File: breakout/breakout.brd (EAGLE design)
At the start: 485 x 130 mm, 229 parts, among them J15 1789472, J16 1789472, J27 69168-124HLF, J30 SJ1-3514-SMT-TR, J32 69168-116HLF, J33 12226-8250-00FR, J34 1888276, J35 69168-116HLF, J36 1888276, Q1 SI1012R, Q2 SI1012R, Q3 SI1012R, Q4 SI1012R, U1 SK6805-E-J, U10 TXB0101, U11 SK6805-E-J, U12 SK6805-E-J, U13 SK6805-E-J, U14 SK6805-E-J, U15 SK6805-E-J, U16 SK6805-E-J, U17 SK6805-E-J, U18 SK6805-E-J, U19 SK6805-E-J, U2 SK6805-E-J, U20 SK6805-E-J, U21 SK6805-E-J, U22 SK6805-E-J, U23 SK6805-E-J, U24 SK6805-E-J, U25 SK6805-E-J, U26 SK6805-E-J, U27 SK6805-E-J, U28 SK6805-E-J, U29 SK6805-E-J, U3 SK6805-E-J, U30 SK6805-E-J, U31 SK6805-E-J, U32 SK6805-E-J, U33 SK6805-E-J, U34 SK6805-E-J, U35 SK6805-E-J, U36 SK6805-E-J, U37 SK6805-E-J, U38 SK6805-E-J, U39 SK6805-E-J, U4 SK6805-E-J, U40 SK6805-E-J, U41 SK6805-E-J, U42 SK6805-E-J, U43 G6K-2F-RF, U44 G6K-2F-RF, U45 G6K-2F-RF, U46 G6K-2F-RF, U47 LTM4622A, U48 SI8610, U49 TINY-FPGA-BX, U5 SK6805-E-J, U50 TCA9555, U51 FIN1032MTCX, U52 SN65LVDS9638DGN, U53 SN65LVDS9638DGN, U6 SK6805-E-J, U7 SK6805-E-J, U8 SK6805-E-J, U9 SK6805-E-J

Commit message: Initial commit of breakout rev 1.4
- Fixes to analog routing to maintain consistancy of analog and digital
pin ordering in the screw terminals and IDC headers
- Switch the ordering of BNC analog connector to row major and aligned
in column direction.
- Add a secondary, internally controlled FET in series with the coil on
each headstage relay so that certain ports can be disabled when
instructed from host.
- Changed the optical table mounting holes to slots that can accomidate
both metric and imperial spacing.
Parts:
- added Q5, Q6, Q7, Q8: SI1012R, jonnew:SC75
- added R35, R37, R39, R41: 100k, jonnew:0402
- added R36, R38, R40, R42: 1k, jonnew:0402
- R11: value 12.5k -> 13.3k
- moved J14 120.8 mm to (240.0, 90.0)
- moved J21 120.8 mm to (40.0, 40.0)
- moved D10 118.8 mm to (260.0, 87.5), turned to 90 degrees
- moved D11 118.8 mm to (60.0, 42.5), turned to 270 degrees
- moved D12 90.0 mm to (100.0, 42.5)
- moved D9 90.0 mm to (220.0, 87.5)
- moved J13 90.0 mm to (200.0, 90.0)
- moved J22 90.0 mm to (80.0, 40.0)
- moved J12 86.0 mm to (160.0, 90.0)
- moved J23 86.0 mm to (120.0, 40.0)
- moved D13 83.2 mm to (140.0, 42.5), turned to 270 degrees
- moved D8 83.2 mm to (180.0, 87.5), turned to 90 degrees
- moved J10 58.3 mm to (80.0, 90.0)
- moved J25 58.3 mm to (200.0, 40.0)
- moved D15 54.1 mm to (220.0, 42.5), turned to 270 degrees
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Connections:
- removed net N$39: D4.C, Q4.2, U46.1
- removed net RELAY_SENSE_0: C28.2, Q1.1, R3.2, U50.6
- removed net RELAY_SENSE_1: C29.2, Q2.1, R4.1, U50.5
- removed net RELAY_SENSE_2: C30.2, Q3.1, R5.1, U50.4
- removed net RELAY_SENSE_3: C31.2, Q4.1, R6.1, U50.20
- new net N$12: D2.A, Q2.3, U44.7
- new net N$50: D3.A, Q3.3, U45.7
- new net N$59: D4.A, Q4.3, U46.7
- new net N$6: Q1.2, Q5.3
- new net N$60: Q4.2, Q8.3
- new net RELAY_AND_0: Q5.1, R36.2, U50.8
- new net RELAY_AND_1: Q6.1, R38.2, U50.6
- new net RELAY_AND_2: Q7.1, R40.2, U50.4
- new net RELAY_AND_3: Q8.1, R42.2, U50.20
- new net RELAY_MECH_0: C28.2, Q1.1, R3.2, R35.2, U50.9
- new net RELAY_MECH_1: C29.2, Q2.1, R37.2, R4.1, U50.7
- new net RELAY_MECH_2: C30.2, Q3.1, R39.2, R5.1, U50.5
- new net RELAY_MECH_3: C31.2, Q4.1, R41.2, R6.1, U50.19
- net +5V0: now also D1.C, D2.C, D3.C, D4.C, U43.1, U44.1, U45.1, U46.1; no longer Q1.3, Q2.3, Q3.3, Q4.3
- net AIO_0: now also J27.2; no longer J27.24
- net AIO_1: now also J27.4; no longer J27.22
- net AIO_10: now also J27.22; no longer J27.4
- net AIO_11: now also J27.24; no longer J27.2
- net AIO_2: now also J27.6; no longer J27.20
- net AIO_3: now also J27.8; no longer J27.18
- net AIO_4: now also J27.10; no longer J27.16
- net AIO_5: now also J27.12; no longer J27.14
- net AIO_6: now also J27.14; no longer J27.12
- net AIO_7: now also J27.16; no longer J27.10
- net AIO_8: now also J27.18; no longer J27.8
- net AIO_9: now also J27.20; no longer J27.6
- net BUTTON1: now also S8.SW1, U50.17; no longer S5.SW1, U50.9
- net BUTTON2: now also S10.SW1, U50.18; no longer S8.SW1, U50.17
- net BUTTON3: now also S5.SW1, U50.11; no longer S7.SW1, U50.14
- net BUTTON4: now also S7.SW1, U50.14; no longer S10.SW1, U50.18
- net BUTTON5: now also U50.10; no longer U50.8
- net GND: now also Q5.2, Q6.2, Q7.2, Q8.2, R35.1, R36.1, R37.1, R38.1, R39.1, R40.1, R41.1, R42.1; no longer D1.A, D2.A, D3.A, D4.A, U43.7, U44.7, U45.7, U46.7
- net N$32: now also Q7.3; no longer D3.C, U45.1
- net N$40: now also Q6.3; no longer D2.C, U44.1
- net N$5: now also D1.A, Q1.3, U43.7; no longer D1.C, Q1.2, U43.1
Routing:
- net RELAY_SENSE_0: track 167.7 -> 0.00 mm, vias 2 -> 0
- net RELAY_MECH_0: track 0.00 -> 164.2 mm, vias 0 -> 4
- net RELAY_AND_0: track 0.00 -> 154.3 mm, vias 0 -> 3
- net AIO_5: track 436.0 -> 282.2 mm, vias 3 -> 2
- net RELAY_MECH_1: track 0.00 -> 149.8 mm, vias 0 -> 4
- net RELAY_MECH_3: track 0.00 -> 145.9 mm, vias 0 -> 4
- net RELAY_AND_1: track 0.00 -> 145.0 mm, vias 0 -> 3
- net RELAY_SENSE_1: track 144.9 -> 0.00 mm, vias 2 -> 0
- net RELAY_AND_3: track 0.00 -> 141.6 mm, vias 0 -> 3
- net RELAY_SENSE_3: track 135.9 -> 0.00 mm, vias 2 -> 0
- net RELAY_MECH_2: track 0.00 -> 130.0 mm, vias 0 -> 4
- net AIO_6: track 400.3 -> 529.8 mm
- net RELAY_AND_2: track 0.00 -> 123.8 mm, vias 0 -> 3
- net RELAY_SENSE_2: track 122.7 -> 0.00 mm, vias 2 -> 0
- net AIO_3: track 471.0 -> 372.4 mm
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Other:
- outline, holes or cut-outs redrawn
- board text added: "(18", 0")"
- board text added: "(200,0)"
- board text added: "(200,100)"
- board text added: "(450,0)"
- board text added: "(8",0")"
- board text added: "Rev. 1.4 CC BY-NC-SA 4.0 JPN, JV, MIT 2019"
- board text removed: "(0",0")"
- board text removed: "(17", 0")"
- board text removed: "(225,0)"
- board text removed: "(425,0)"
- board text removed: "Rev. 1.3 CERN OHL v1.2 JPN, JV, MIT 2019"

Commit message: Changes to breakout rev 1.4 after case fit test with rev 1.3
- Moved components to prevent them from being smashed by case
- More clearance around M3 holes
- Smaller font on analog BNC labels
- Moved the terminal blocks so that there spacing makes more sense for
related signals.
- Modeled screw terminal blocks correctly
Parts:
- removed TP8: (no value), jonnew:TP19R
- R11: value 13.3k -> 1k
- R12: value 649k -> 100k
- R13: value 8.25k -> 1k
- R14, R16: value 4.7k -> 100k
- R15: value 4.7k -> 1k
- R17: value 100 -> 1k
- R18: value 100 -> 100k
- R19: value 270, 0.5W -> 13.3k; device jonnew:0805 -> jonnew:0402
- R20: value 270, 0.5W -> 649k; device jonnew:0805 -> jonnew:0402
- R21: value 270, 0.5W -> 8.25k; device jonnew:0805 -> jonnew:0402
- R22, R23, R24: value 270, 0.5W -> 4.7k; device jonnew:0805 -> jonnew:0402
- R25, R26: value 270, 0.5W -> 100; device jonnew:0805 -> jonnew:0402
- R35, R37, R39, R41: value 100k -> 270, 0.5W; device jonnew:0402 -> jonnew:0805
- R36, R38, R40, R42: value 1k -> 270, 0.5W; device jonnew:0402 -> jonnew:0805
- TP7: device jonnew:TESTPOINT_2MM -> jonnew:TP19R
- moved TP7 228.0 mm to (456.1, 78.2)
- moved R35 178.2 mm to (469.3, 111.3), turned to 180 degrees
- moved R37 168.1 mm to (472.9, 111.3), turned to 180 degrees
- moved TP5 164.3 mm to (295.0, 4.90)
- moved R39 163.1 mm to (476.5, 111.3), turned to 180 degrees
- moved R41 161.9 mm to (480.1, 111.3), turned to 180 degrees
- moved R36 148.2 mm to (432.9, 114.4), turned to 180 degrees
- moved R12 138.3 mm to (317.4, 18.1), turned to 90 degrees
- moved R18 137.9 mm to (319.2, 93.3)
- moved R11 136.5 mm to (320.2, 18.1), turned to 90 degrees
- moved R17 135.3 mm to (322.0, 93.3), turned to 90 degrees
- moved R13 133.9 mm to (322.0, 43.3), turned to 90 degrees
- moved R38 129.6 mm to (432.9, 110.4), turned to 180 degrees
- moved R15 128.2 mm to (322.0, 68.2), turned to 90 degrees
- moved R16 127.2 mm to (319.2, 68.2), turned to 90 degrees
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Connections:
- net !TCA_INT: now also R22.2; no longer R14.2
- net +12V: now also TP7.TP; no longer TP8.TP
- net +3V3: now also R22.1, R23.1, R24.1; no longer R14.1, R15.1, R16.1
- net AGND: now also TP6.1; no longer TP7.1
- net BUTTON0: now also S5.SW1; no longer S6.SW1
- net BUTTON1: now also S7.SW1; no longer S8.SW1
- net BUTTON2: now also S9.SW1; no longer S10.SW1
- net BUTTON3: now also S6.SW1; no longer S5.SW1
- net BUTTON4: now also S8.SW1; no longer S7.SW1
- net BUTTON5: now also S10.SW1; no longer S9.SW1
- net DIN0: now also R42.2; no longer R34.2
- net DIN0_P: now also R42.1; no longer R34.1
- net DIN1: now also R34.2; no longer R26.2
- net DIN1_P: now also R34.1; no longer R26.1
- net DIN2: now also R40.2; no longer R32.2
- net DIN2_P: now also R40.1; no longer R32.1
- net DIN3: now also R32.2; no longer R24.2
- net DIN3_P: now also R32.1; no longer R24.1
- net DIN4: now also R38.2; no longer R30.2
- net DIN4_P: now also R38.1; no longer R30.1
- net DIN5: now also R30.2; no longer R22.2
- net DIN5_P: now also R30.1; no longer R22.1
- net DIN6: now also R36.2; no longer R28.2
- net DIN6_P: now also R36.1; no longer R28.1
- net DIN7: now also R28.2; no longer R20.2
- net DIN7_P: now also R28.1; no longer R20.1
- net DOUT0: now also D21.2, R27.2; no longer D21.10, R19.2
- net DOUT0_P: now also R27.1; no longer R19.1
- net DOUT1: now also D21.1, R29.2; no longer D21.9, R21.2
- net DOUT1_P: now also R29.1; no longer R21.1
- net DOUT2: now also D21.3, R31.2; no longer D21.2, R23.2
- net DOUT2_P: now also R31.1; no longer R23.1
- net DOUT3: now also D21.4, R33.2; no longer D21.7, R25.2
- net DOUT3_P: now also R33.1; no longer R25.1
- net DOUT4: now also D21.10, R35.2; no longer D21.3, R27.2
- net DOUT4_P: now also R35.1; no longer R27.1
- net DOUT5: now also D21.9, R37.2; no longer D21.6, R29.2
- net DOUT5_P: now also R37.1; no longer R29.1
- net DOUT6: now also D21.7, R39.2; no longer D21.4, R31.2
- net DOUT6_P: now also R39.1; no longer R31.1
- net DOUT7: now also D21.6, R41.2; no longer D21.1, R33.2
- net DOUT7_P: now also R41.1; no longer R33.1
- net GND: now also R11.1, R12.1, R13.1, R14.1, R15.1, R16.1, R17.1, R18.1, R19.2, R20.2, R21.2; no longer R11.2, R12.2, R13.2, R35.1, R36.1, R37.1, R38.1, R39.1, R40.1, R41.1, R42.1, TP6.1
- net I2C_SCL: now also R23.2; no longer R15.2
- net I2C_SDA: now also R24.2; no longer R16.2
- net LVDS_DOUT0_N: now also R25.1; no longer R17.1
- net LVDS_DOUT0_P: now also R25.2; no longer R17.2
- net LVDS_DOUT1_N: now also R26.1; no longer R18.1
- net LVDS_DOUT1_P: now also R26.2; no longer R18.2
- net N$145: now also R20.1; no longer R12.1
- net N$24: now also R21.1; no longer R13.1
- net N$25: now also R19.1; no longer R11.1
- net RELAY_AND_0: now also R11.2; no longer R36.2
- net RELAY_AND_1: now also R13.2; no longer R38.2
- net RELAY_AND_2: now also R15.2; no longer R40.2
- net RELAY_AND_3: now also R17.2; no longer R42.2
- net RELAY_MECH_0: now also R12.2; no longer R35.2
- net RELAY_MECH_1: now also R14.2; no longer R37.2
- net RELAY_MECH_2: now also R16.2; no longer R39.2
- net RELAY_MECH_3: now also R18.2; no longer R41.2
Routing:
- net DOUT7: track 63.8 -> 86.6 mm
- net DOUT6: track 63.4 -> 83.4 mm
- net DIN1: track 93.6 -> 83.7 mm
- net DIN0: track 82.8 -> 73.2 mm
- net DIN4: track 68.6 -> 61.2 mm
- net DOUT1: track 52.6 -> 45.8 mm
- net DIN6: track 64.3 -> 57.9 mm
- net DIN5: track 74.3 -> 68.1 mm
- net DIN2: track 73.7 -> 67.6 mm
- net DOUT3: track 62.7 -> 56.6 mm
- net DOUT4: track 65.0 -> 70.6 mm
- net DIN3: track 80.7 -> 75.1 mm
- net DOUT5: track 69.1 -> 74.1 mm
- net DOUT0: track 48.8 -> 44.4 mm
- net DOUT1_P: track 6.23 -> 9.69 mm
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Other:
- board text added: "GPIO"
- board text removed: "DIGITAL IO"

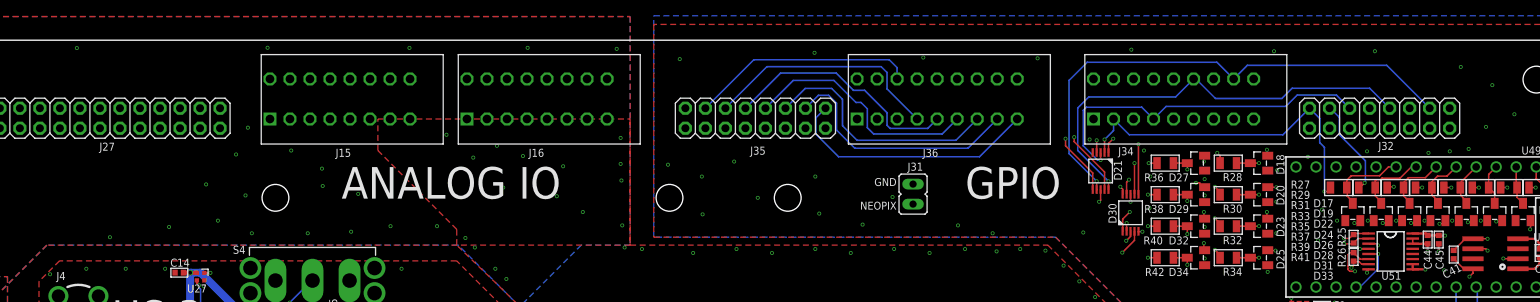
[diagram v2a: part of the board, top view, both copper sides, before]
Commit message: Minore updates to breakout rev 1.4
- Address issues found during the construction of the case
- DOUT IDC and terminal block switch positions to match the other two IO
banks
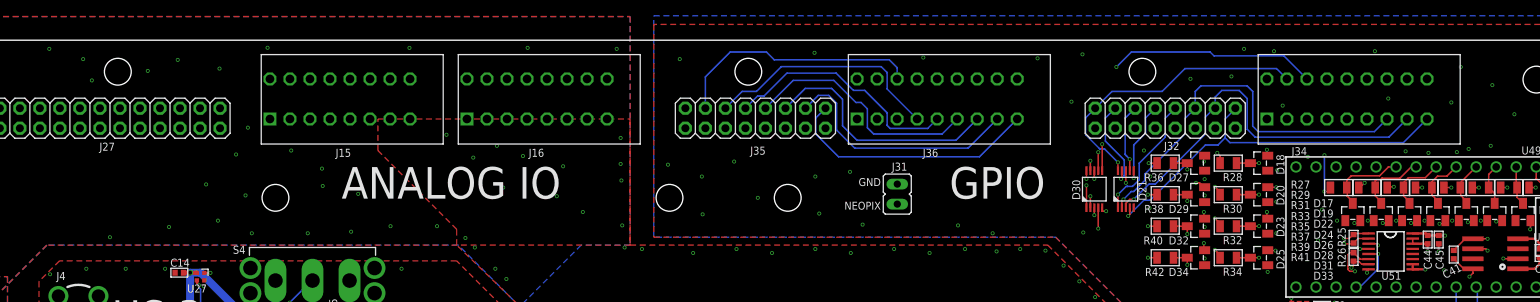
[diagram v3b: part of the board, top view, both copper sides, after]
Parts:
- moved J32 27.2 mm to (432.9, 120.0)
- moved J34 22.0 mm to (445.8, 120.0)
- moved D30 5.49 mm to (423.9, 111.1)
- moved D21 3.94 mm to (427.9, 111.1), turned to 90 degrees
- moved J31 2.00 mm to (398.9, 109.2)
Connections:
- net DOUT0: now also D21.10; no longer D21.2
- net DOUT1: now also D21.9; no longer D21.1
- net DOUT2: now also D21.7; no longer D21.3
- net DOUT3: now also D21.6; no longer D21.4
- net DOUT4: now also D21.1; no longer D21.10
- net DOUT5: now also D21.2; no longer D21.9
- net DOUT6: now also D21.3; no longer D21.7
- net DOUT7: now also D21.4; no longer D21.6
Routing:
- net DOUT7: track 86.6 -> 70.6 mm
- net DOUT6: track 83.4 -> 70.6 mm
- net DOUT4: track 70.6 -> 58.3 mm
- net DOUT1: track 45.8 -> 56.9 mm, vias 2 -> 3
- net DOUT2: track 58.1 -> 50.4 mm
- net DOUT5: track 74.1 -> 66.6 mm
- net DOUT0: track 44.4 -> 50.0 mm, vias 2 -> 3
- net DOUT3: track 56.6 -> 51.6 mm
- net DIN7: track 68.1 -> 64.5 mm
- net DIN1: track 83.7 -> 87.1 mm
- net DIN0: track 73.2 -> 75.9 mm
- net NEOPIXEL_DIN: track 53.8 -> 55.8 mm
- net DIN6: track 57.9 -> 56.2 mm
- net AIO_2: track 411.6 -> 413.0 mm
- net AIO_0: track 485.5 -> 484.2 mm
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
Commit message: More updates to breakout rev. 1.4 to fit case
- Swiched 2x 8 pin screw terminals for a single 16 pin screw terminal.
- Moved m3 clearance holes in front of IDC connectors up a bit
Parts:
- removed J36: 1888276, jonnew:SCREW9-2
- J15: value 1789472 -> (none); device jonnew:SCREW8-2 -> jonnew:MMCX-THRU
- J16: value 1789472 -> (none); device jonnew:SCREW8-2 -> jonnew:SMA_JACK_142-0701-201
- J17: value (none) -> 1789074; device jonnew:MMCX-THRU -> jonnew:SCREW16-2
- J18: device jonnew:SMA_JACK_142-0701-201 -> jonnew:MMCX-THRU
- J19, J28: device jonnew:MMCX-THRU -> jonnew:SMA_JACK_142-0701-201
- J20: device jonnew:SMA_JACK_142-0701-201 -> jonnew:0731010360
- J26: value (none) -> 69168-124HLF; device jonnew:0731010360 -> jonnew:2X12-BIG
- J27: value 69168-124HLF -> (none); device jonnew:2X12-BIG -> jonnew:MMCX-THRU
- J29: value (none) -> SJ1-3514-SMT-TR; device jonnew:SMA_JACK_142-0701-201 -> jonnew:35RASMT2BHNTRX
- J30: value SJ1-3514-SMT-TR -> (none); device jonnew:35RASMT2BHNTRX -> jonnew:JP2
- J31: value (none) -> 69168-116HLF; device jonnew:JP2 -> jonnew:2X08-BIG
- J32: value 69168-116HLF -> 12226-8250-00FR; device jonnew:2X08-BIG -> jonnew:12226-82X0-00XX
- J33: value 12226-8250-00FR -> 1888276; device jonnew:12226-82X0-00XX -> jonnew:SCREW9-2
- J34: value 1888276 -> 69168-116HLF; device jonnew:SCREW9-2 -> jonnew:2X08-BIG
- J35: value 69168-116HLF -> 1888276; device jonnew:2X08-BIG -> jonnew:SCREW9-2
- moved J20 340.6 mm to (40.0, 40.0)
- moved J27 211.8 mm to (480.0, 10.0)
- moved J17 190.4 mm to (318.0, 120.0)
- moved J15 189.3 mm to (480.0, 20.0)
- moved J29 139.3 mm to (479.9, 91.0), turned to 180 degrees
- moved J28 120.4 mm to (360.0, 20.0)
- moved J16 114.5 mm to (400.0, 20.0)
- moved J26 100.4 mm to (300.6, 120.0)
- moved J19 100.1 mm to (380.0, 20.0)
- moved J30 83.0 mm to (398.9, 109.2), turned to 90 degrees
- moved J18 80.2 mm to (480.0, 15.0)
- moved J32 72.4 mm to (480.0, 65.0), turned to 90 degrees
- moved J34 67.4 mm to (378.4, 120.0)
- moved J33 64.8 mm to (445.8, 120.0), turned to 0 degrees
- moved J21 40.0 mm to (80.0, 40.0)
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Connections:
- net +12V: now also J32.1, J32.26; no longer J33.1, J33.26
- net AGND: now also J17.1, J17.15, J17.16, J17.17, J17.18, J17.2, J17.31, J17.32, J20.2, J20.3, J20.4, J20.5, J26.1, J26.11, J26.13, J26.15, J26.17, J26.19, J26.21, J26.23, J26.7, J26.9, J32.13, J32.14; no longer J15.1, J15.10, J15.2, J15.9, J16.1, J16.10, J16.2, J16.9, J26.2, J26.4, J27.1, J27.11, J27.13, J27.15, J27.17, J27.19, J27.21, J27.23, J27.3, J27.5, J27.7, J27.9, J33.13, J33.14
- net AIO_0: now also J17.19, J17.3, J26.2, J32.20; no longer J15.11, J15.3, J27.2, J33.20
- net AIO_1: now also J17.20, J17.4, J26.4, J32.7; no longer J15.12, J15.4, J27.4, J33.7
- net AIO_10: now also J17.13, J17.29, J24.1, J26.22, J32.15; no longer J16.15, J16.7, J25.1, J27.22, J33.15
- net AIO_11: now also J17.14, J17.30, J25.1, J26.24, J32.2; no longer J16.16, J16.8, J26.1, J27.24, J33.2
- net AIO_2: now also J17.21, J17.5, J26.6, J32.19; no longer J15.13, J15.5, J27.6, J33.19
- net AIO_3: now also J17.22, J17.6, J26.8, J32.6; no longer J15.14, J15.6, J27.8, J33.6
- net AIO_4: now also J17.23, J17.7, J26.10, J32.18; no longer J15.15, J15.7, J27.10, J33.18
- net AIO_5: now also J17.24, J17.8, J26.12, J32.5; no longer J15.16, J15.8, J27.12, J33.5
- net AIO_6: now also J17.25, J17.9, J20.1, J26.14, J32.17; no longer J16.11, J16.3, J21.1, J27.14, J33.17
- net AIO_7: now also J17.10, J17.26, J21.1, J26.16, J32.4; no longer J16.12, J16.4, J22.1, J27.16, J33.4
- net AIO_8: now also J17.11, J17.27, J22.1, J26.18, J32.16; no longer J16.13, J16.5, J23.1, J27.18, J33.16
- net AIO_9: now also J17.12, J17.28, J23.1, J26.20, J32.3; no longer J16.14, J16.6, J24.1, J27.20, J33.3
- net DIN0: now also J34.2, J35.11; no longer J36.11, J36.2
- net DIN1: now also J34.4, J35.12, J35.3; no longer J35.4, J36.12, J36.3
- net DIN2: now also J34.6, J35.13, J35.4; no longer J35.6, J36.13, J36.4
- net DIN3: now also J34.8, J35.14, J35.5; no longer J35.8, J36.14, J36.5
- net DIN4: now also J34.10, J35.15, J35.6; no longer J35.10, J36.15, J36.6
- net DIN5: now also J34.12, J35.16, J35.7; no longer J35.12, J36.16, J36.7
- net DIN6: now also J34.14, J35.17, J35.8; no longer J35.14, J36.17, J36.8
- net DIN7: now also J34.16, J35.18, J35.9; no longer J35.16, J36.18, J36.9
- net DOUT0: now also J31.2, J33.11, J33.2; no longer J32.2, J34.11, J34.2
- net DOUT1: now also J31.4, J33.12, J33.3; no longer J32.4, J34.12, J34.3
- net DOUT2: now also J31.6, J33.13, J33.4; no longer J32.6, J34.13, J34.4
- net DOUT3: now also J31.8, J33.14, J33.5; no longer J32.8, J34.14, J34.5
- net DOUT4: now also J31.10, J33.15, J33.6; no longer J32.10, J34.15, J34.6
- net DOUT5: now also J31.12, J33.16, J33.7; no longer J32.12, J34.16, J34.7
- net DOUT6: now also J31.14, J33.17, J33.8; no longer J32.14, J34.17, J34.8
- net DOUT7: now also J31.16, J33.18, J33.9; no longer J32.16, J34.18, J34.9
- net GND: now also J15.GND@1, J15.GND@2, J15.GND@3, J15.GND@4, J16.GND$1, J16.GND$2, J16.GND$3, J16.GND$4, J18.GND@1, J18.GND@2, J18.GND@3, J18.GND@4, J19.GND$1, J19.GND$2, J19.GND$3, J19.GND$4, J27.GND@1, J27.GND@2, J27.GND@3, J27.GND@4, J28.GND$1, J28.GND$2, J28.GND$3, J28.GND$4, J30.2, J31.1, J31.11, J31.13, J31.15, J31.3, J31.5, J31.7, J31.9, J32.PAD1, J32.PAD2, J33.1, J33.10, J34.11, J34.13, J34.15, J34.3, J34.5, J34.7, J34.9, J35.10; no longer J17.GND@1, J17.GND@2, J17.GND@3, J17.GND@4, J18.GND$1, J18.GND$2, J18.GND$3, J18.GND$4, J19.GND@1, J19.GND@2, J19.GND@3, J19.GND@4, J20.GND$1, J20.GND$2, J20.GND$3, J20.GND$4, J28.GND@1, J28.GND@2, J28.GND@3, J28.GND@4, J29.GND$1, J29.GND$2, J29.GND$3, J29.GND$4, J31.2, J32.1, J32.11, J32.13, J32.15, J32.3, J32.5, J32.7, J32.9, J33.PAD1, J33.PAD2, J34.10, J35.11, J35.13, J35.15, J35.3, J35.5, J35.7, J35.9, J36.1, J36.10
- net LVDS_DIN0_N: now also J32.23; no longer J33.23
- net LVDS_DIN0_P: now also J32.10; no longer J33.10
- net LVDS_DIN1_N: now also J32.11; no longer J33.11
- net LVDS_DIN1_P: now also J32.24; no longer J33.24
- net LVDS_DIN2_N: now also J32.25; no longer J33.25
- net LVDS_DIN2_P: now also J32.12; no longer J33.12
- net LVDS_DOUT0_N: now also J32.8; no longer J33.8
- net LVDS_DOUT0_P: now also J32.21; no longer J33.21
- net LVDS_DOUT1_N: now also J32.9; no longer J33.9
- net LVDS_DOUT1_P: now also J32.22; no longer J33.22
- net N$1: now also J15.SIG, J16.CLK; no longer J17.SIG, J18.CLK
- net N$16: now also J29.1; no longer J30.1
- net N$17: now also J29.5; no longer J30.5
- net N$18: now also J29.4; no longer J30.4
- net N$3: now also J18.SIG, J19.CLK; no longer J19.SIG, J20.CLK
- net N$4: now also J27.SIG, J28.CLK; no longer J28.SIG, J29.CLK
- net NEOPIXEL_DIN: now also J30.1; no longer J31.1
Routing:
- net AIO_8: track 453.4 -> 445.6 mm
- net AIO_9: track 414.3 -> 406.7 mm
- net AIO_10: track 375.3 -> 367.7 mm
- net AIO_6: track 529.9 -> 522.9 mm
- net AIO_7: track 491.2 -> 484.4 mm
- net AIO_11: track 335.3 -> 329.5 mm
- net DOUT1: track 56.9 -> 52.7 mm
- net DIN7: track 64.5 -> 67.3 mm
- net DIN6: track 56.2 -> 59.0 mm
- net DIN5: track 67.8 -> 70.3 mm
- net DIN2: track 68.0 -> 70.5 mm
- net DIN3: track 75.1 -> 77.5 mm
- net DIN4: track 61.7 -> 64.2 mm
- net AIO_3: track 372.4 -> 374.1 mm
- net AIO_0: track 484.2 -> 482.8 mm
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
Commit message: Breakout board rev. 1.5
- Very minor changes to 1.4 after a full fit test.
- The M6/14-20 mount slots were made larger
- The M3 holes were turned into slots to allow some slop
- The power neopixel was moved down by 3.5 mm
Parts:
- TP7: device jonnew:TP19R -> jonnew:TESTPOINT_2MM
- moved C3 3.00 mm to (472.0, 76.2)
- moved R1 3.00 mm to (467.1, 76.1)
- moved U1 3.00 mm to (469.8, 76.2)
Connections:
- net +12V: now also TP7.1; no longer TP7.TP
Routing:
- net +5V0: track 1317.8 -> 1320.8 mm
- net N$21: track 166.6 -> 165.0 mm
- net N$55: track 27.5 -> 28.8 mm
- net AIO_11: track 329.5 -> 328.3 mm
- net LVDS_DOUT0_P: track 65.7 -> 66.8 mm
- net LVDS_DOUT0_N: track 65.4 -> 66.5 mm
- net LVDS_DOUT1_P: track 67.8 -> 68.7 mm
- net LVDS_DOUT1_N: track 64.6 -> 65.4 mm
- net N$48: track 34.7 -> 34.1 mm
- net +12V: track 55.6 -> 55.4 mm, vias 15 -> 14
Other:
- outline, holes or cut-outs redrawn
- board text added: "Rev. 1.5 CC BY-NC-SA 4.0 JPN, JV, MIT 2020"
- board text removed: "Rev. 1.4 CC BY-NC-SA 4.0 JPN, JV, MIT 2019"
